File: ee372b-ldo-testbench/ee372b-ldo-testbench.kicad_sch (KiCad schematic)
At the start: 128 parts, among them J1 PEC02SAAN, J10 OUT_S, J11 VOUT, J12 VDD_BUF, J13 V_SIG, J14 PEC03SAAN, J15 VSIG_BUF, J16 PEC03SAAN, J17 PEC03SAAN, J18 PEC03SAAN, J19 PEC03SAAN, J2 PEC02SAAN, J20 VREF_EXTERNAL, J21 PEC02SAAN, J22 PEC02SAAN, J23 PEC02SAAN, J24 PEC02SAAN, J25 PEC03SAAN, J3 GND, J4 1V8, J5 3v3_EXTERNAL, J6 GND, J9 IN_S, Q1 FDV305N, Q2 FDV305N, Q3 FDV305N, Q4 FDV305N, Q5 FDV305N, U1 MMSZ4679T1G, U3 ADS1220IPW, U4 BUF634AIDR

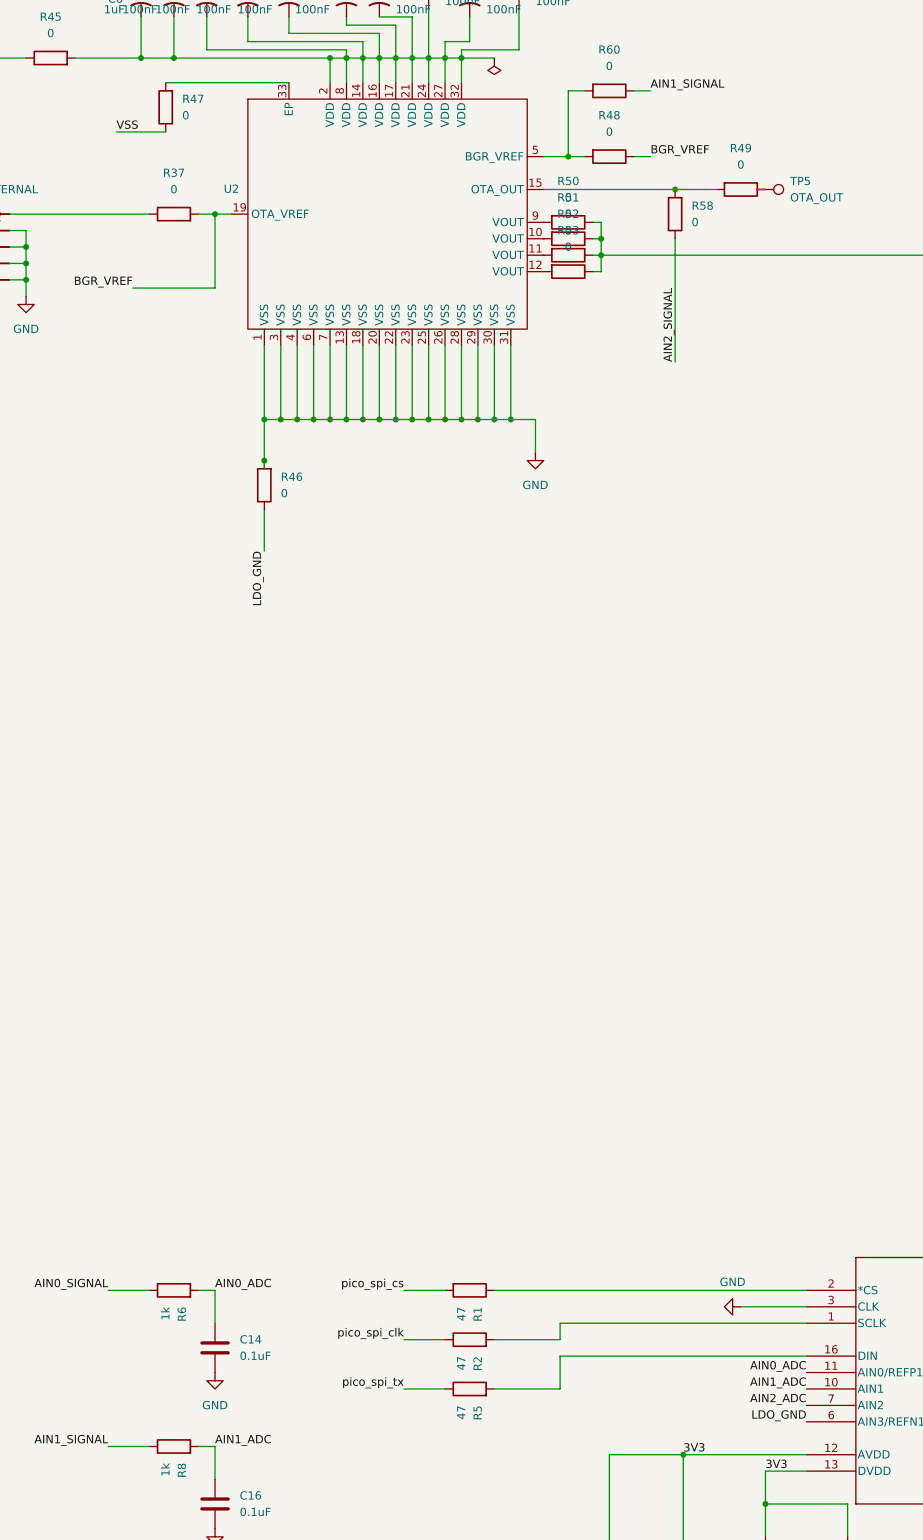
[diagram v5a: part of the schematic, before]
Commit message: first plane fill on L2 GND
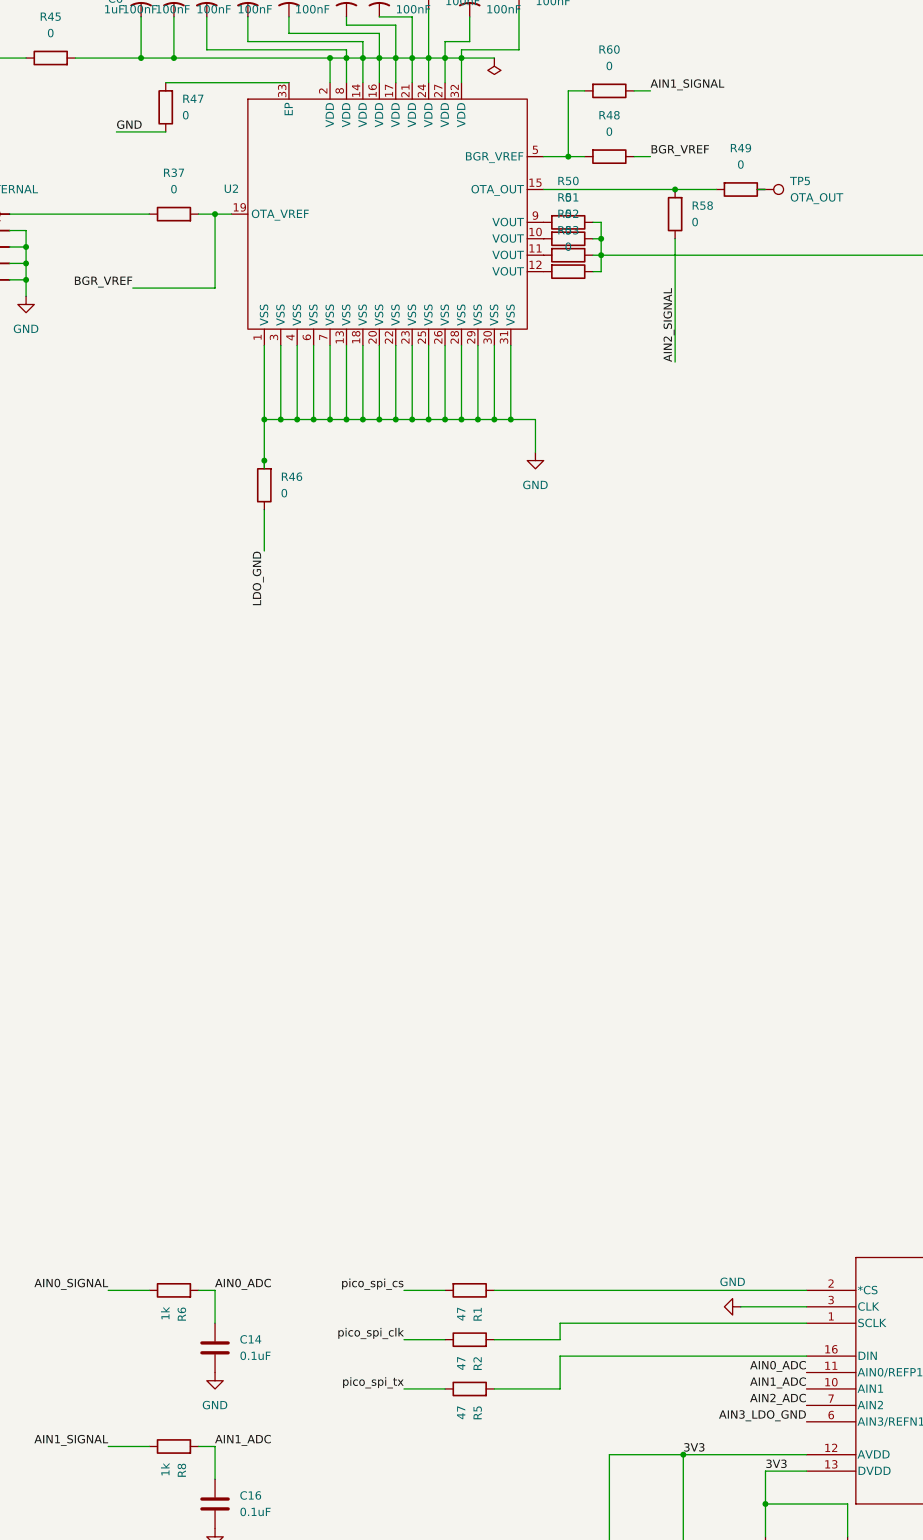
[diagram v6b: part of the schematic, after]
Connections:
- net VSS is gone; now on net GND: R47.1
- net LDO_GND: no longer U3.6 (AIN3/REFN1)
- new net AIN3_LDO_GND: U3.6 (AIN3/REFN1)
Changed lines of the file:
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@@
 		)
 	)
-	(label "VSS"
+	(label "GND"
 		(at 321.31 91.44 0)
 		(effects
@@
 		)
 	)
-	(label "LDO_GND"
+	(label "AIN3_LDO_GND"
 		(at 427.99 290.83 180)
 		(effects

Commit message: fixed last ERC issues
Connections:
- net LDO_GND is gone; now on net AIN3_LDO_GND: R46.1
- net 3V3_EXTERNAL: now also C28.1, J5.1 (Pin_1), TP10.1
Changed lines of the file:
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@@
 	)
 	(junction
+		(at 256.54 208.28)
+		(diameter 0)
+		(color 0 0 0 0)
+	)
+	(junction
 		(at 307.34 111.76)
 		(diameter 0)
@@
 	)
 	(junction
+		(at 256.54 240.03)
+		(diameter 0)
+		(color 0 0 0 0)
+	)
+	(junction
 		(at 344.17 142.24)
 		(diameter 0)
@@
 	(wire
 		(pts
-			(xy 254 208.28) (xy 260.35 208.28)
+			(xy 254 208.28) (xy 256.54 208.28)
 		)
 		(stroke
@@
 	(wire
 		(pts
-			(xy 246.38 240.03) (xy 264.16 240.03)
+			(xy 246.38 240.03) (xy 256.54 240.03)
 		)
 		(stroke
@@
 	(wire
 		(pts
+			(xy 256.54 208.28) (xy 260.35 208.28)
+		)
+		(stroke
+			(width 0)
+			(type default)
+		)
+	)
+	(wire
+		(pts
 			(xy 120.65 335.28) (xy 127 335.28)
 		)
@@
 	(wire
 		(pts
+			(xy 256.54 240.03) (xy 264.16 240.03)
+		)
+		(stroke
+			(width 0)
+			(type default)
+		)
+	)
+	(wire
+		(pts
 			(xy 344.17 149.86) (xy 344.17 156.21)
 		)
@@
 	(wire
 		(pts
+			(xy 256.54 208.28) (xy 256.54 240.03)
+		)
+		(stroke
+			(width 0)
+			(type default)
+		)
+	)
+	(wire
+		(pts
 			(xy 394.97 107.95) (xy 396.24 107.95)
 		)
@@
 		)
 	)
-	(label "LDO_GND"
+	(label "AIN3_LDO_GND"
 		(at 344.17 156.21 270)
 		(effects
